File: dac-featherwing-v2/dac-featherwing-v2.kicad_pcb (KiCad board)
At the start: 2 copper layers, 43.2 x 58.4 mm, 36 parts, among them J1 BOT, J2 TOP, J3 AudioJack4, J4 AudioJack4, U1 WM8731CLSEFL

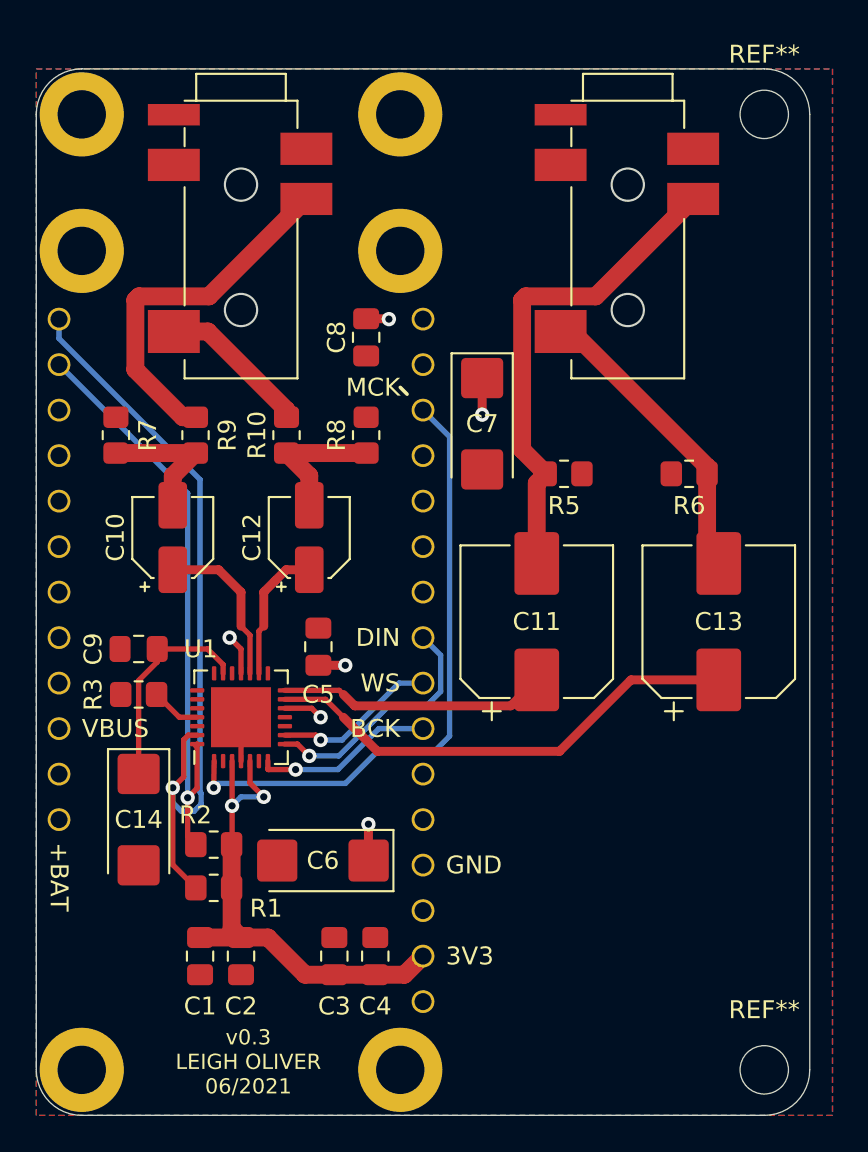
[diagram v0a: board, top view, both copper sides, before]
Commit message: Minor updates to ground plane
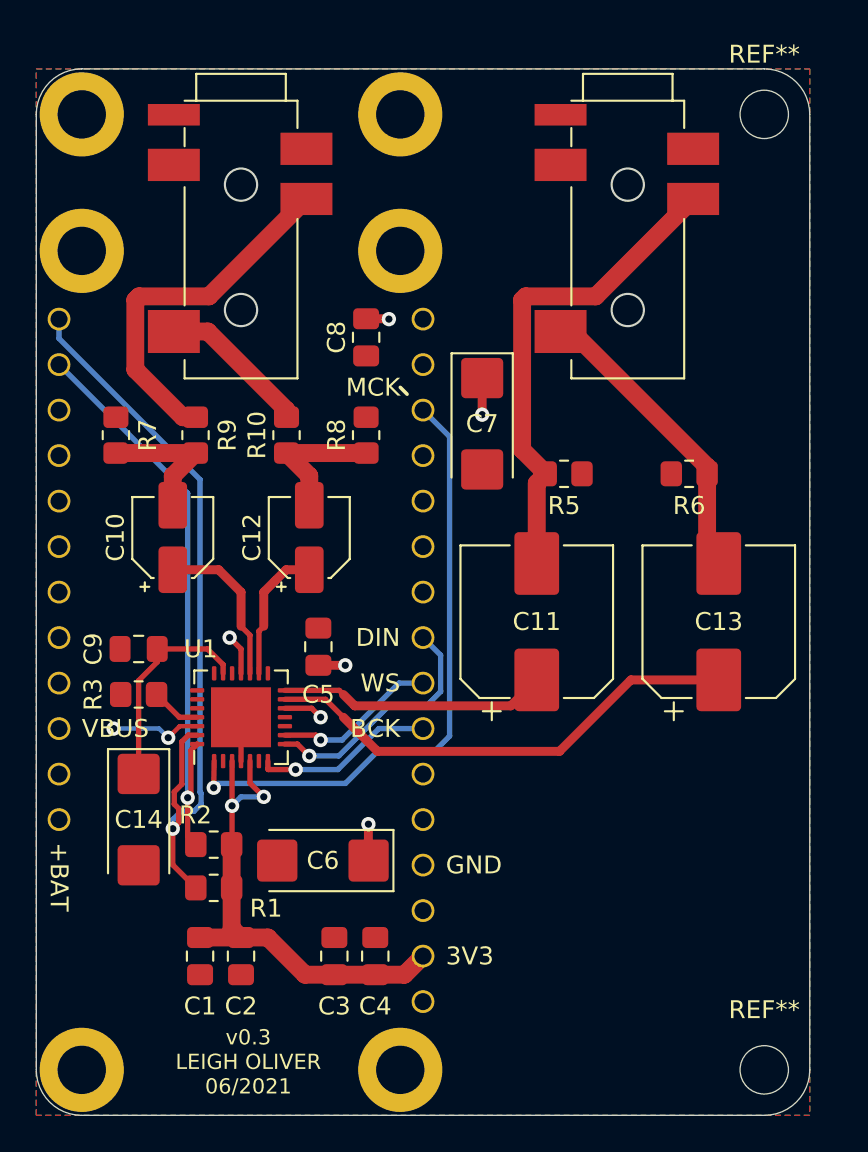
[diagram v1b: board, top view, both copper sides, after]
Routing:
- net GND: track 2.45 -> 7.59 mm, vias 0 -> 2
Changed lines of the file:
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@@
   (segment (start 119.424 89.181) (end 119.424 88.691242) (width 0.3) (layer "F.Cu") (net 1))
   (segment (start 117.445636 98.288636) (end 117.9 98.743) (width 0.3) (layer "F.Cu") (net 13))
-  (segment (start 117.974 95.59406) (end 117.974 93.131) (width 0.3) (layer "F.Cu") (net 13))
   (segment (start 117.445636 96.122424) (end 117.445636 98.288636) (width 0.3) (layer "F.Cu") (net 13))
-  (segment (start 117.445636 96.122424) (end 117.974 95.59406) (width 0.3) (layer "F.Cu") (net 13))
+  (segment (start 117.63 93.475) (end 117.974 93.131) (width 0.3) (layer "F.Cu") (net 13))
+  (segment (start 117.445636 96.122424) (end 117.63 95.93806) (width 0.3) (layer "F.Cu") (net 13))
   (segment (start 117.974 93.131) (end 117.884 93.221) (width 0.3) (layer "F.Cu") (net 13))
+  (segment (start 117.63 95.93806) (end 117.63 93.475) (width 0.3) (layer "F.Cu") (net 13))
   (via (at 117.445636 96.122424) (size 0.8) (drill 0.4) (layers "F.Cu" "B.Cu") (net 13))
   (segment (start 110.264 71.946) (end 117.445636 79.127636) (width 0.3) (layer "B.Cu") (net 13))
   (segment (start 117.445636 79.127636) (end 117.445636 96.122424) (width 0.3) (layer "B.Cu") (net 13))
+  (segment (start 116.946116 96.732181) (end 116.696125 96.48219) (width 0.3) (layer "F.Cu") (net 14))
+  (segment (start 116.614 99.87) (end 117.9 101.156) (width 0.3) (layer "F.Cu") (net 14))
+  (segment (start 117.122 95.372913) (end 117.122 92.993242) (width 0.3) (layer "F.Cu") (net 14))
+  (segment (start 116.696125 95.798788) (end 117.122 95.372913) (width 0.3) (layer "F.Cu") (net 14))
+  (segment (start 116.696125 96.48219) (end 116.696125 95.798788) (width 0.3) (layer "F.Cu") (net 14))
+  (segment (start 116.614 97.854) (end 116.614 99.87) (width 0.3) (layer "F.Cu") (net 14))
   (segment (start 117.484242 92.631) (end 117.974 92.631) (width 0.3) (layer "F.Cu") (net 14))
-  (segment (start 116.614 99.87) (end 117.9 101.156) (width 0.3) (layer "F.Cu") (net 14))
-  (segment (start 117.22448 92.890762) (end 117.484242 92.631) (width 0.3) (layer "F.Cu") (net 14))
-  (segment (start 116.614 95.568) (end 116.614 99.87) (width 0.3) (layer "F.Cu") (net 14))
-  (segment (start 116.614 95.568) (end 117.22448 94.95752) (width 0.3) (layer "F.Cu") (net 14))
-  (segment (start 117.22448 94.95752) (end 117.22448 92.890762) (width 0.3) (layer "F.Cu") (net 14))
-  (via (at 116.614 95.568) (size 0.8) (drill 0.4) (layers "F.Cu" "B.Cu") (net 14))
+  (segment (start 116.614 97.854) (end 116.946116 97.521884) (width 0.3) (layer "F.Cu") (net 14))
+  (segment (start 117.122 92.993242) (end 117.484242 92.631) (width 0.3) (layer "F.Cu") (net 14))
+  (segment (start 116.946116 97.521884) (end 116.946116 96.732181) (width 0.3) (layer "F.Cu") (net 14))
+  (via (at 116.614 97.854) (size 0.8) (drill 0.4) (layers "F.Cu" "B.Cu") (net 14))
+  (segment (start 117.08587 96.871935) (end 117.805402 96.871935) (width 0.3) (layer "B.Cu") (net 14))
+  (segment (start 116.614 97.854) (end 116.614 97.343805) (width 0.3) (layer "B.Cu") (net 14))
+  (segment (start 118.195147 96.48219) (end 118.195147 95.879147) (width 0.3) (layer "B.Cu") (net 14))
+  (segment (start 118.138 78.362923) (end 110.264 70.488923) (width 0.3) (layer "B.Cu") (net 14))
+  (segment (start 117.805402 96.871935) (end 118.195147 96.48219) (width 0.3) (layer "B.Cu") (net 14))
+  (segment (start 116.614 97.343805) (end 117.08587 96.871935) (width 0.3) (layer "B.Cu") (net 14))
   (segment (start 110.264 70.488923) (end 110.264 69.406) (width 0.3) (layer "B.Cu") (net 14))
-  (segment (start 116.614 96.400065) (end 117.08587 96.871935) (width 0.3) (layer "B.Cu") (net 14))
-  (segment (start 117.805402 96.871935) (end 118.195147 96.48219) (width 0.3) (layer "B.Cu") (net 14))
-  (segment (start 118.195147 96.48219) (end 118.195147 95.879147) (width 0.3) (layer "B.Cu") (net 14))
+  (segment (start 118.195147 95.879147) (end 118.138 95.822) (width 0.3) (layer "B.Cu") (net 14))
   (segment (start 118.138 95.822) (end 118.138 78.362923) (width 0.3) (layer "B.Cu") (net 14))
-  (segment (start 117.08587 96.871935) (end 117.805402 96.871935) (width 0.3) (layer "B.Cu") (net 14))
-  (segment (start 116.614 95.568) (end 116.614 96.400065) (width 0.3) (layer "B.Cu") (net 14))
-  (segment (start 118.138 78.362923) (end 110.264 70.488923) (width 0.3) (layer "B.Cu") (net 14))
-  (segment (start 118.195147 95.879147) (end 118.138 95.822) (width 0.3) (layer "B.Cu") (net 14))
   (segment (start 120.424 87.821) (end 119.789 87.186) (width 0.3) (layer "F.Cu") (net 15))
   (segment (start 124.742 88.7315) (end 126.2445 88.7315) (width 0.5) (layer "F.Cu") (net 15))
@@
   (segment (start 128.115428 92.266) (end 125.829428 94.552) (width 0.3) (layer "B.Cu") (net 23))
   (segment (start 120.424 94.081) (end 120.424 91.631) (width 0.3) (layer "F.Cu") (net 26))
+  (segment (start 117.003 92.131) (end 117.974 92.131) (width 0.25) (layer "F.Cu") (net 26))
+  (segment (start 116.36 92.774) (end 117.003 92.131) (width 0.25) (layer "F.Cu") (net 26))
+  (via (at 113.312 92.266) (size 0.8) (drill 0.4) (layers "F.Cu" "B.Cu") (net 26))
+  (via (at 116.36 92.774) (size 0.8) (drill 0.4) (layers "F.Cu" "B.Cu") (net 26))
+  (segment (start 115.852 92.266) (end 113.312 92.266) (width 0.25) (layer "B.Cu") (net 26))
+  (segment (start 116.36 92.774) (end 115.852 92.266) (width 0.25) (layer "B.Cu") (net 26))
   (segment (start 121.9265 103.9285) (end 124.0015 106.0035) (width 1) (layer "F.Cu") (net 28))
   (segment (start 119.924 98.719) (end 119.9 98.743) (width 0.3) (layer "F.Cu") (net 28))
@@
     (polygon
       (pts
-        (xy 153.444 113.856)
+        (xy 152.174 113.856)
         (xy 108.994 113.856)
         (xy 108.994 55.436)
-        (xy 153.444 55.436)
+        (xy 152.174 55.436)
       )
     )
@@
     (polygon
       (pts
-        (xy 153.444 113.856)
+        (xy 152.174 113.856)
         (xy 108.994 113.856)
         (xy 108.994 55.436)
-        (xy 153.444 55.436)
+        (xy 152.174 55.436)
       )
     )
